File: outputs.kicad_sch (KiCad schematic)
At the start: 64 parts, among them J1 AudioJack2_SwitchT, J2 AudioJack2_SwitchT, J3 AudioJack2_SwitchT, J4 AudioJack2_SwitchT, J5 AudioJack2_SwitchT, J6 AudioJack2_SwitchT, J7 AudioJack2_SwitchT, J8 AudioJack2_SwitchT, U34 AD5754R, U35 AD5754R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

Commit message: pcb changes
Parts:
- R13, R14, R15, R16, R21, R22, R23, R24: value 10M -> 1M; LCSC Part # C7250 -> C22935
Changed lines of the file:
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@@
 			)
 		)
-		(property "Value" "10M"
+		(property "Value" "1M"
 			(at 50.8 57.1499 0)
 			(effects
@@
 			)
 		)
-		(property "LCSC Part #" "C7250"
+		(property "LCSC Part #" "C22935"
 			(at 48.26 55.88 0)
 			(effects
@@
 			)
 		)
-		(property "Value" "10M"
+		(property "Value" "1M"
 			(at 50.8 33.0199 0)
 			(effects
@@
 			)
 		)
-		(property "LCSC Part #" "C7250"
+		(property "LCSC Part #" "C22935"
 			(at 48.26 31.75 0)
 			(effects
@@
 			)
 		)
-		(property "Value" "10M"
+		(property "Value" "1M"
 			(at 168.91 109.2199 0)
 			(effects
@@
 			)
 		)
-		(property "LCSC Part #" "C7250"
+		(property "LCSC Part #" "C22935"
 			(at 166.37 107.95 0)
 			(effects
@@
 			)
 		)
-		(property "Value" "10M"
+		(property "Value" "1M"
 			(at 168.91 58.4199 0)
 			(effects
@@
 			)
 		)
-		(property "LCSC Part #" "C7250"
+		(property "LCSC Part #" "C22935"
 			(at 166.37 57.15 0)
 			(effects
@@
 			)
 		)
-		(property "Value" "10M"
+		(property "Value" "1M"
 			(at 50.8 107.9499 0)
 			(effects
@@
 			)
 		)
-		(property "LCSC Part #" "C7250"
+		(property "LCSC Part #" "C22935"
 			(at 48.26 106.68 0)
 			(effects
@@
 			)
 		)
-		(property "Value" "10M"
+		(property "Value" "1M"
 			(at 168.91 83.8199 0)
 			(effects
@@
 			)
 		)
-		(property "LCSC Part #" "C7250"
+		(property "LCSC Part #" "C22935"
 			(at 166.37 82.55 0)
 			(effects
@@
 			)
 		)
-		(property "Value" "10M"
+		(property "Value" "1M"
 			(at 50.8 82.5499 0)
 			(effects
@@
 			)
 		)
-		(property "LCSC Part #" "C7250"
+		(property "LCSC Part #" "C22935"
 			(at 48.26 81.28 0)
 			(effects
@@
 			)
 		)
-		(property "Value" "10M"
+		(property "Value" "1M"
 			(at 168.91 34.2899 0)
 			(effects
@@
 			)
 		)
-		(property "LCSC Part #" "C7250"
+		(property "LCSC Part #" "C22935"
 			(at 166.37 33.02 0)
 			(effects

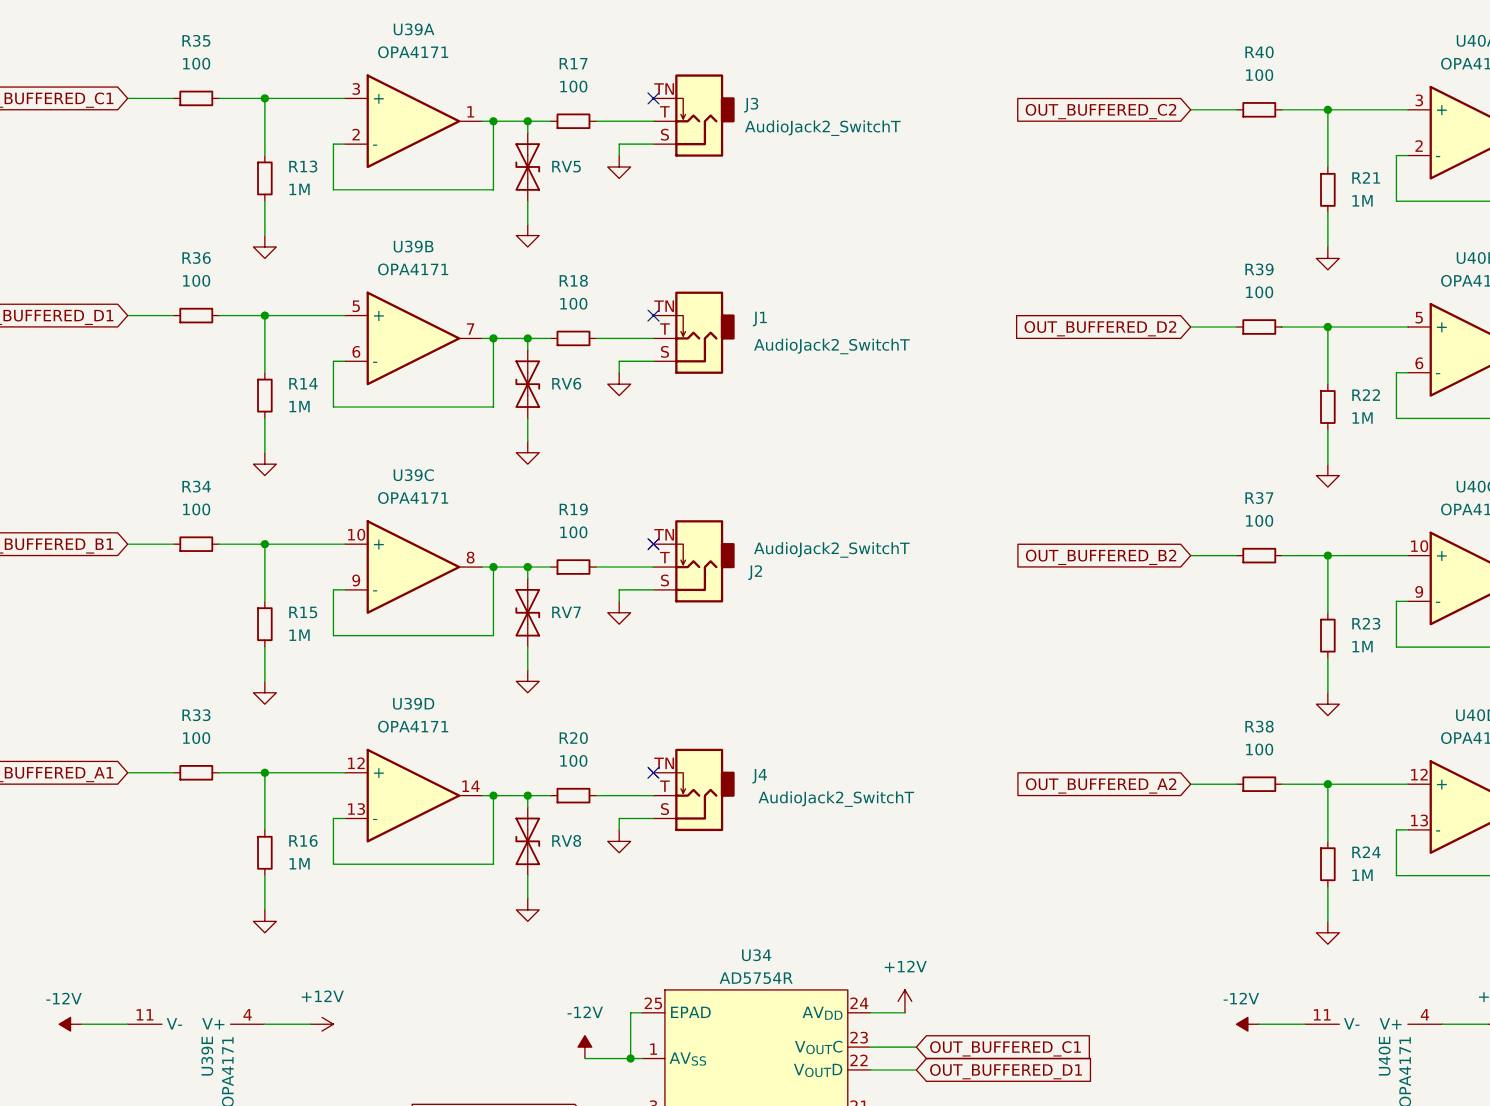
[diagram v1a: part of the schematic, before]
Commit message: RC filters on DAC output
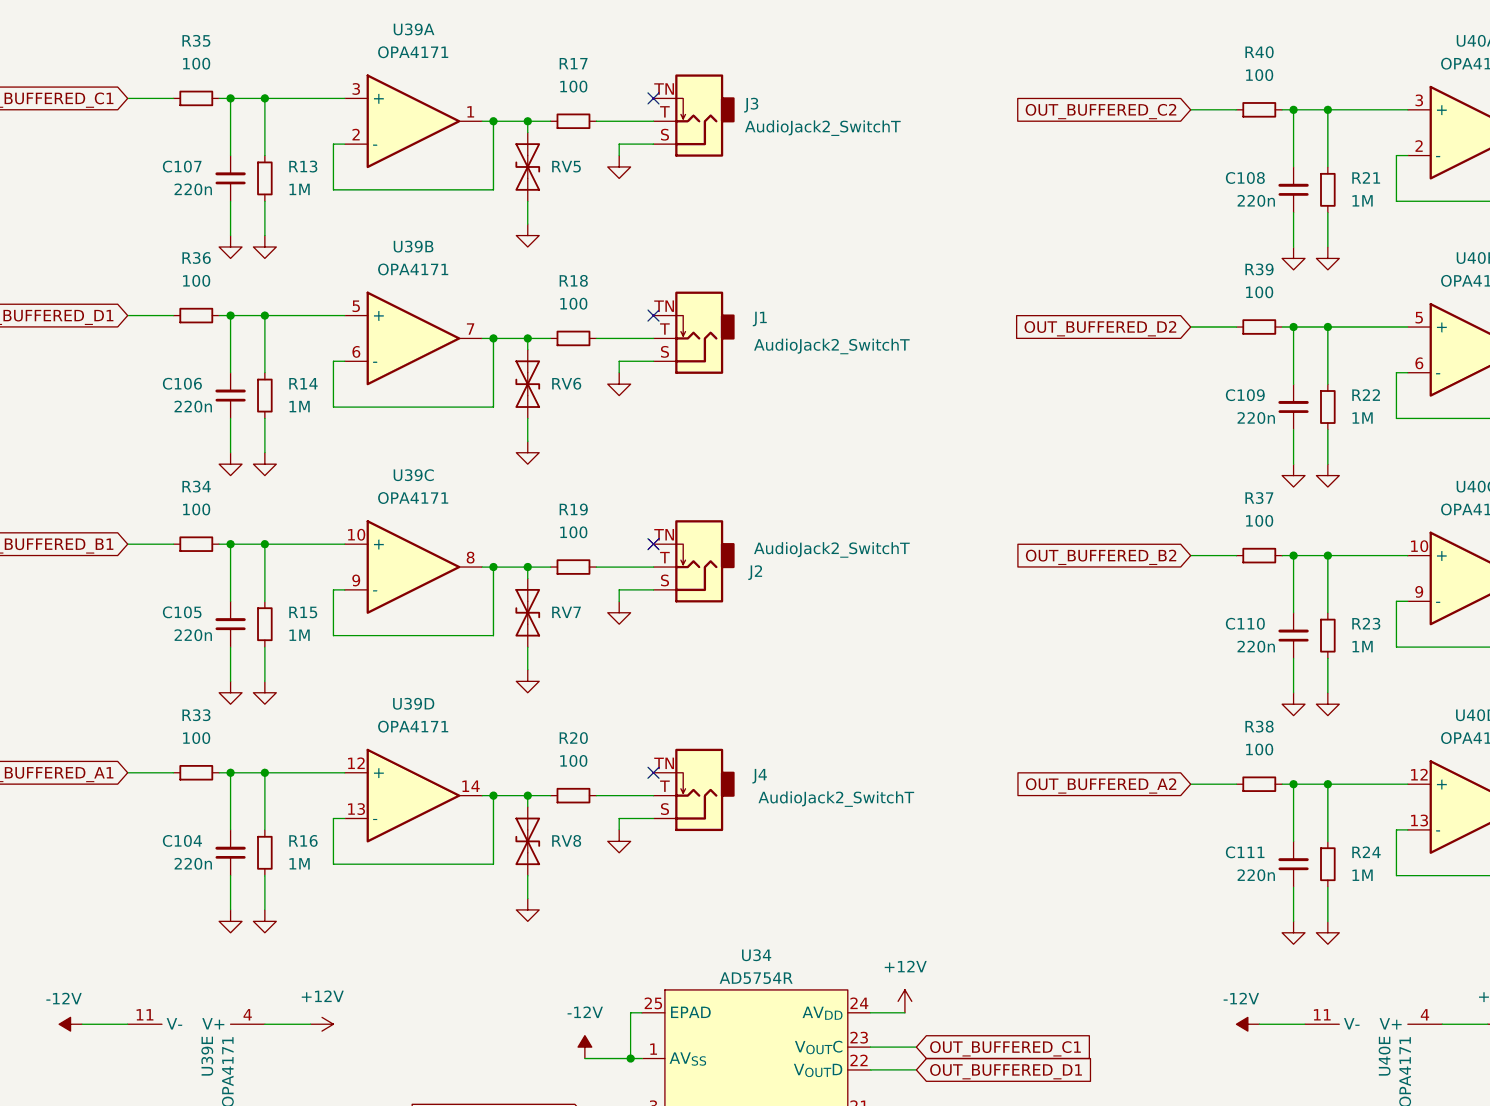
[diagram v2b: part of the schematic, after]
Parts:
- added C104, C105, C106, C107, C108, C109, C110, C111: 220n, Capacitor_SMD:C_0402_1005Metric, symbol Device:C_Small
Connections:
- net GND: now also C104.1, C105.1, C106.1, C107.1, C108.1, C109.1, C110.1, C111.1
- net at R21.1, R40.2, U40.3 (+): now also C108.2
- net at R16.1, R33.2, U39.12 (+): now also C104.2
- net at R14.1, R36.2, U39.5 (+): now also C106.2
- net at R24.1, R38.2, U40.12 (+): now also C111.2
- net at R22.1, R39.2, U40.5 (+): now also C109.2
- net at R13.1, R35.2, U39.3 (+): now also C107.2
- net at R15.1, R34.2, U39.10 (+): now also C105.2
- net at R23.1, R37.2, U40.10 (+): now also C110.2

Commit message: v1
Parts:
- U34, U35: LCSC Part # C392906 -> C392905
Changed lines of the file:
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@@
 			)
 		)
-		(property "LCSC Part #" "C392906"
+		(property "LCSC Part #" "C392905"
 			(at 237.49 139.7 0)
 			(effects
@@
 			)
 		)
-		(property "LCSC Part #" "C392906"
+		(property "LCSC Part #" "C392905"
 			(at 102.87 143.51 0)
 			(effects
